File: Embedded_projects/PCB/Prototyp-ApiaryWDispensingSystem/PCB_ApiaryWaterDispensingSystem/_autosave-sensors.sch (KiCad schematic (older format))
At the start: 25 parts

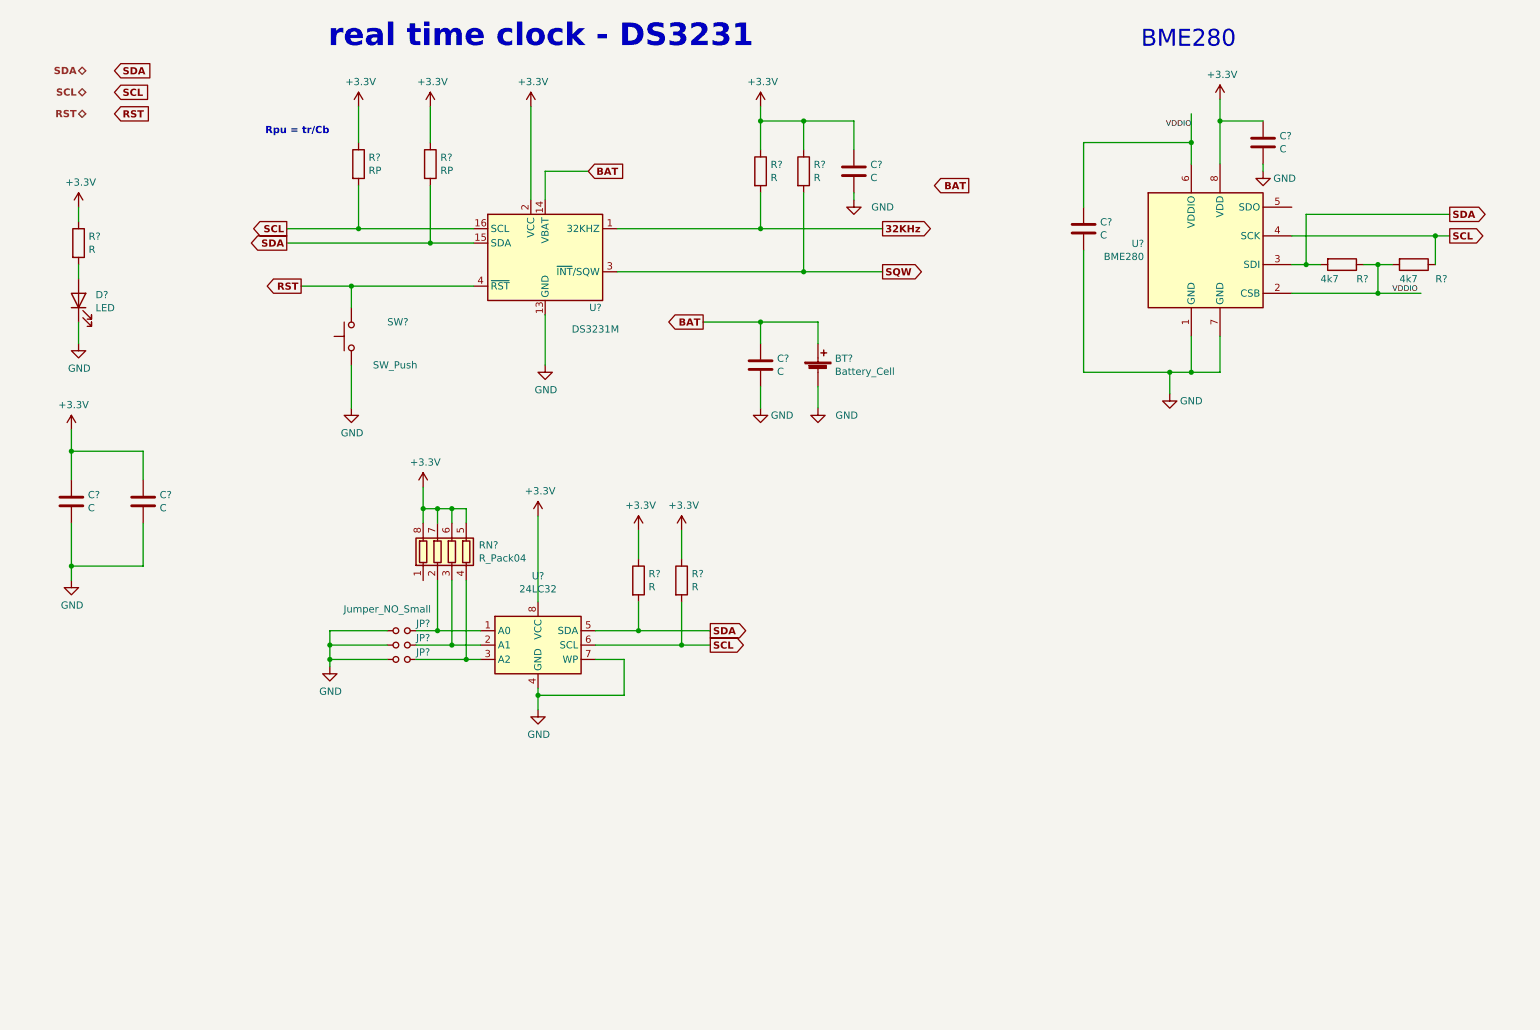
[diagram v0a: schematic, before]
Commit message: added ina219 to the project #3
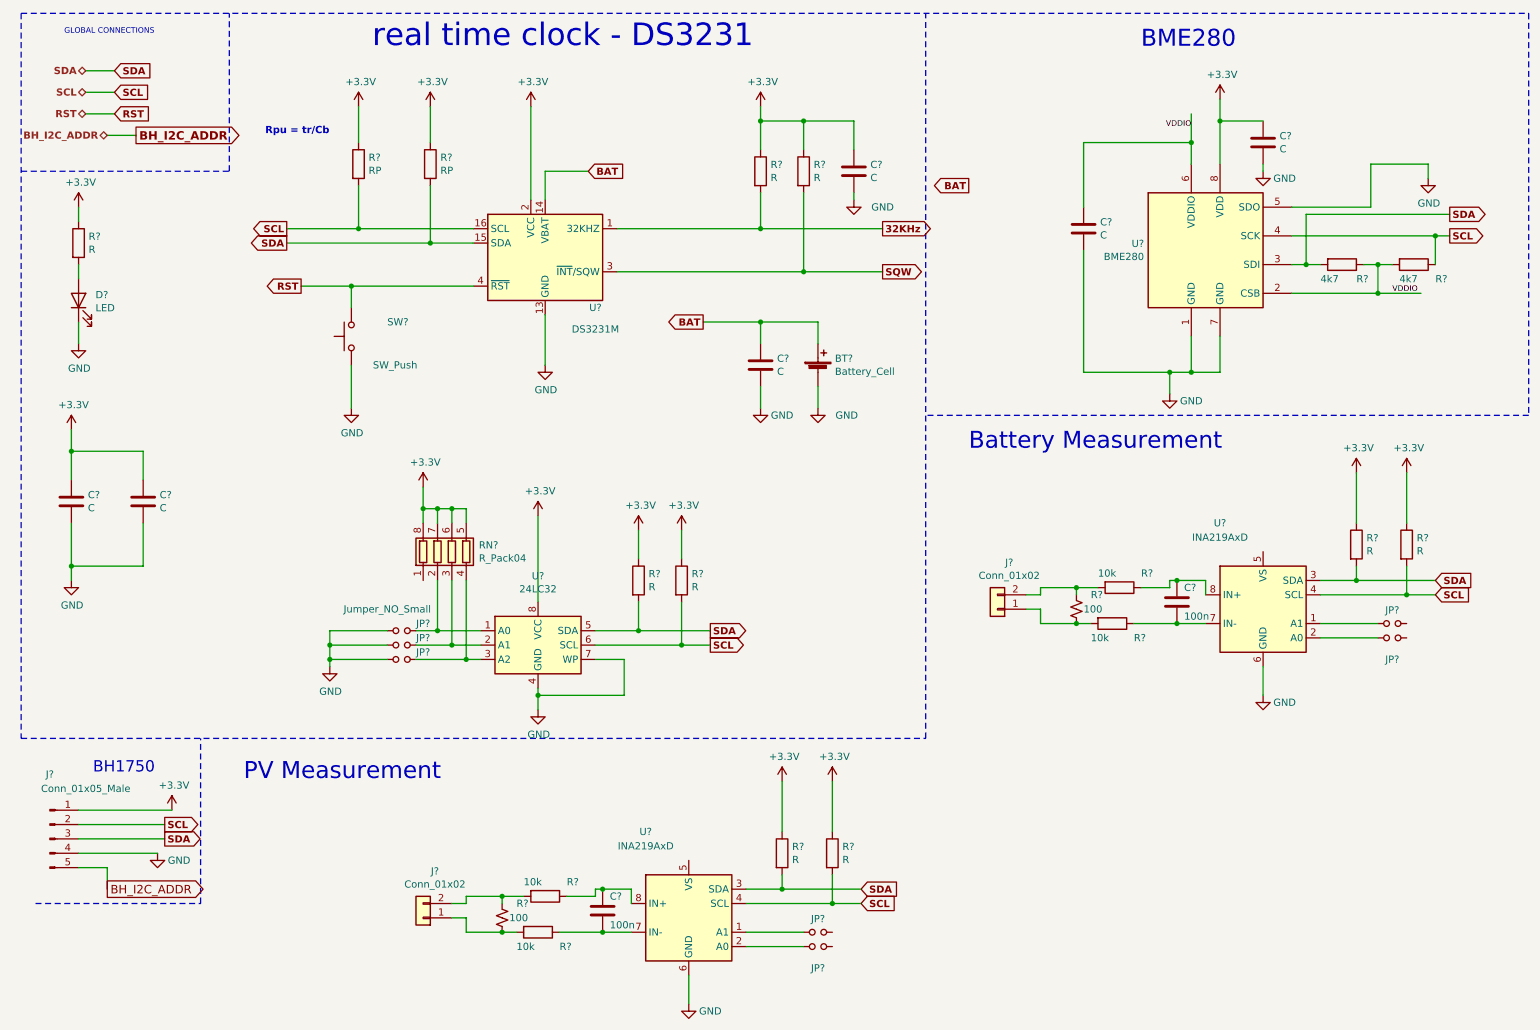
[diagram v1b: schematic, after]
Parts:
- added C? (x2): 100n, symbol Device:C
- added J?: Conn_01x05_Male, symbol Connector:Conn_01x05_Male
- added J? (x2): Conn_01x02, symbol Connector_Generic:Conn_01x02
- added JP? (x4): Jumper_NO_Small, symbol Device:Jumper_NO_Small
- added R? (x4): R, symbol Device:R
- added R? (x2): 100, symbol Device:R_Small_US
- added R? (x4): 10k, symbol Device:R
- added U? (x2): INA219AxD, Package_SO:SOIC-8_3.9x4.9mm_P1.27mm, symbol Analog_ADC:INA219AxD
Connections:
- net +3V3: now also J?.1 (Pin_1), R?.1, R?.1, R?.1, R?.1
- net GND: now also U?.5 (SDO), J?.4 (Pin_4), U?.6 (GND), U?.6 (GND)
- net SCL: now also J?.2 (Pin_2), R?.2, R?.2, U?.4 (SCL), U?.4 (SCL)
- net SDA: now also J?.3 (Pin_3), R?.2, R?.2, U?.3 (SDA), U?.3 (SDA)
- new net: JP?.1, U?.1 (A1) (x2)
- new net: JP?.1, U?.2 (A0) (x2)
- new net: C?.2, R?.1, U?.7 (IN-) (x2)
- new net: C?.1, R?.1, U?.8 (IN+) (x2)
- new net: J?.2 (Pin_2), R?.1, R?.2 (x2)
- new net: J?.1 (Pin_1), R?.2, R?.2 (x2)
- new net BH_I2C_ADDR: J?.5 (Pin_5)
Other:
- note added: "BH1750"
- note added: "Battery Measurement"
- note added: "GLOBAL CONNECTIONS"
- note added: "PV Measurement"
